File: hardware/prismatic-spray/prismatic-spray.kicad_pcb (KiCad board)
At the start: 2 copper layers, 205.3 x 86 mm, 17 parts, among them J1 Conn_01x03_Male, J2 Conn_01x03_Male, SW1 SW_Push, SW2 SW_Push, SW3 SW_Push, SW4 SW_Push, SW5 RotaryEncoder_Switch, U1 Pico

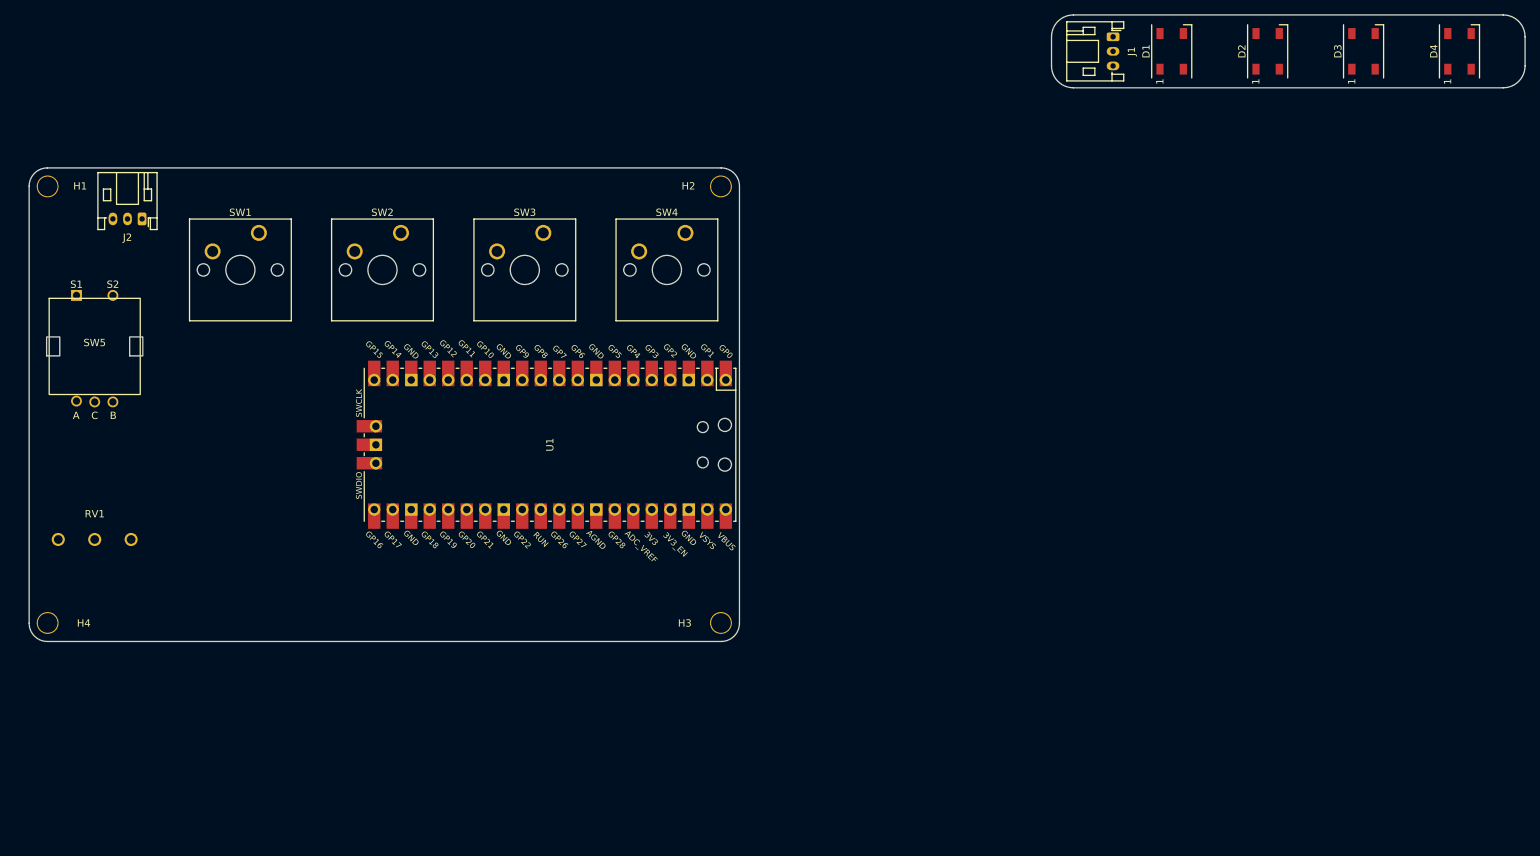
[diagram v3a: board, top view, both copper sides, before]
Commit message: Route most traces
- Route most traces on main board and daughter board
- Add mounting holes to daughter board
- Flip daughterboard connector to back of PCB
- Reassign some GPIOs for better routing
- Fix footprint for pec11 to get clean DRC
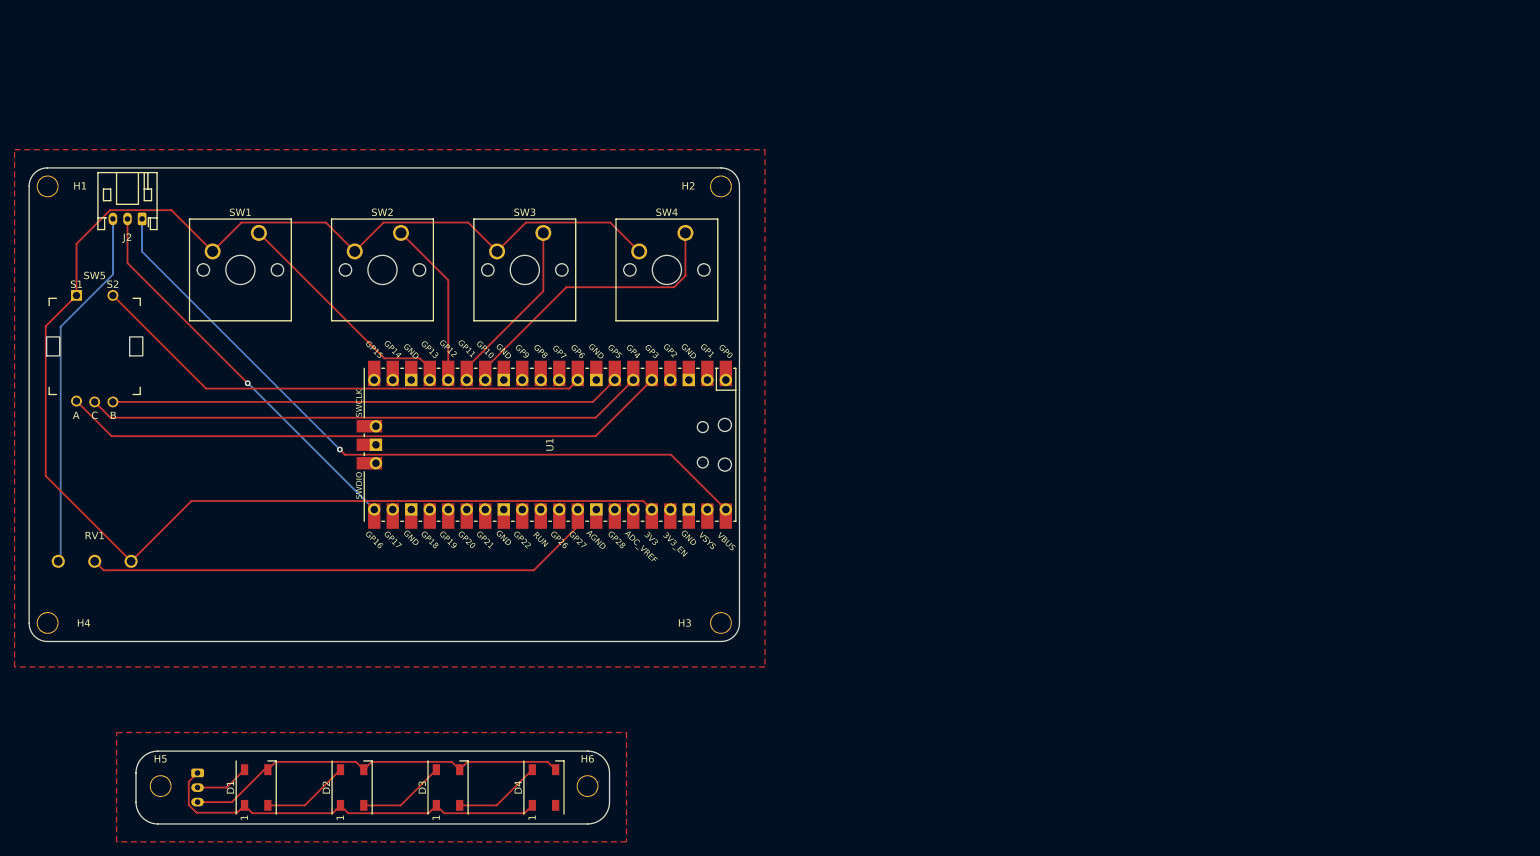
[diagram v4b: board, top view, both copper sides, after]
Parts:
- added H5: MountingHole, MountingHole:MountingHole_2.7mm_M2.5, F.Cu at (53.0, 125.3)
- added H6: MountingHole, MountingHole:MountingHole_2.7mm_M2.5, F.Cu at (111.7, 125.3)
- J1: moved to B.Cu
- moved D1 161.3 mm to (66.2, 125.5)
- moved D2 161.3 mm to (79.3, 125.5)
- moved D4 161.3 mm to (105.7, 125.5)
- moved D3 161.3 mm to (92.5, 125.5)
- moved J1 161.3 mm to (58.1, 123.5)
- moved RV1 3.00 mm to (44.0, 94.5)
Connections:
- net Net-(D1-Pad1) renamed /5V_B
- net Net-(D1-Pad3) renamed /GND_B
- D1 pad 4: /DATA -> /DATA_B
- J1 pad 2: /DATA -> /DATA_B
- J2 pad 1: +5V -> /5V_A
- J2 pad 2: /DATA -> /DATA_A
- SW5 pad A: Net-(U1-Pad7) -> Net-(U1-Pad5)
- SW5 pad B: Net-(U1-Pad5) -> Net-(U1-Pad7)
- SW5 pad S2: Net-(U1-Pad4) -> Net-(U1-Pad9)
- U1 pad 21: /DATA -> /DATA_A
- U1 pad 36: unconnected-(U1-Pad36) -> +3V3
- U1 pad 38: GND -> unconnected-(U1-Pad38)
- U1 pad 4: Net-(U1-Pad4) -> unconnected-(U1-Pad4)
- U1 pad 40: unconnected-(U1-Pad40) -> /5V_A
- U1 pad 9: unconnected-(U1-Pad9) -> Net-(U1-Pad9)
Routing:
- net +3V3: track 0.00 -> 216.9 mm
- net /5V_A: track 0.00 -> 99.3 mm, vias 0 -> 1
- net Net-(U1-Pad5): track 0.00 -> 84.2 mm
- net Net-(U1-Pad6): track 0.00 -> 77.0 mm
- net Net-(RV1-Pad2): track 0.00 -> 71.6 mm
- net Net-(U1-Pad7): track 0.00 -> 70.1 mm
- net Net-(U1-Pad9): track 0.00 -> 69.6 mm
- net /5V_B: track 0.00 -> 55.6 mm
- net /DATA_A: track 0.00 -> 53.9 mm, vias 0 -> 1
- net /GND_B: track 0.00 -> 53.7 mm
- net GND: track 0.00 -> 50.1 mm
- net Net-(SW4-Pad1): track 0.00 -> 40.2 mm
- net Net-(SW1-Pad1): track 0.00 -> 32.8 mm
- net Net-(SW3-Pad1): track 0.00 -> 24.5 mm
- net Net-(SW2-Pad1): track 0.00 -> 22.9 mm
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- added copper zone on F.Cu, net GND
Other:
- board size 205.3 x 86 mm -> 97.5 x 90.1 mm

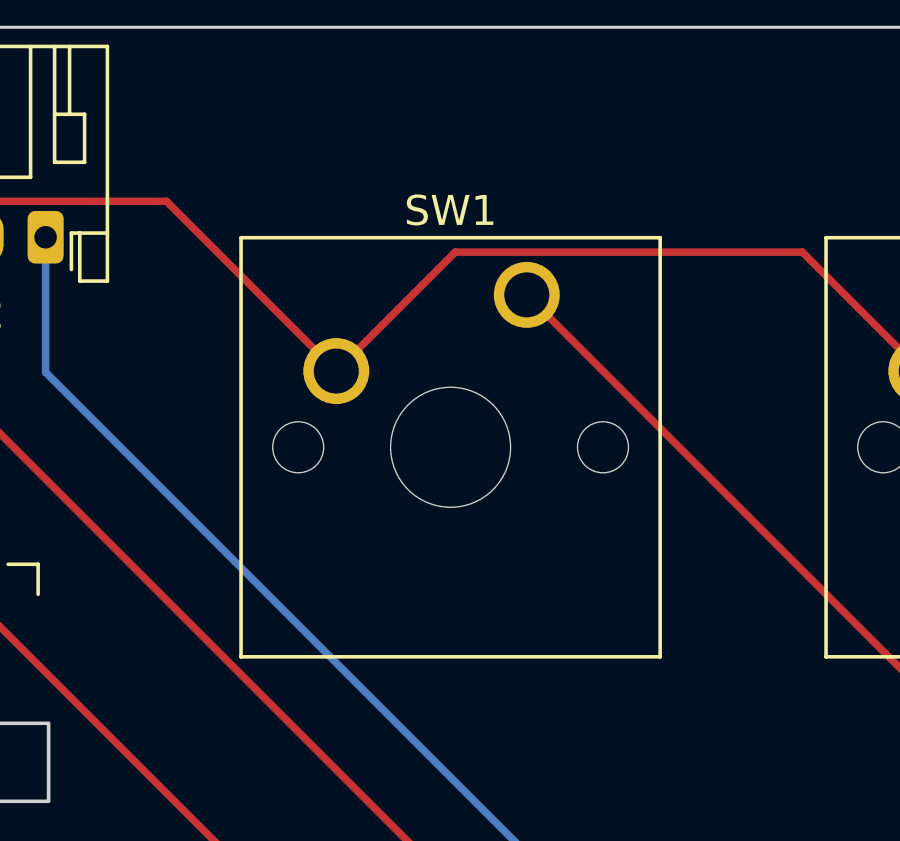
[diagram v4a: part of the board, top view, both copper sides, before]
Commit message: Add dimentions to PCB
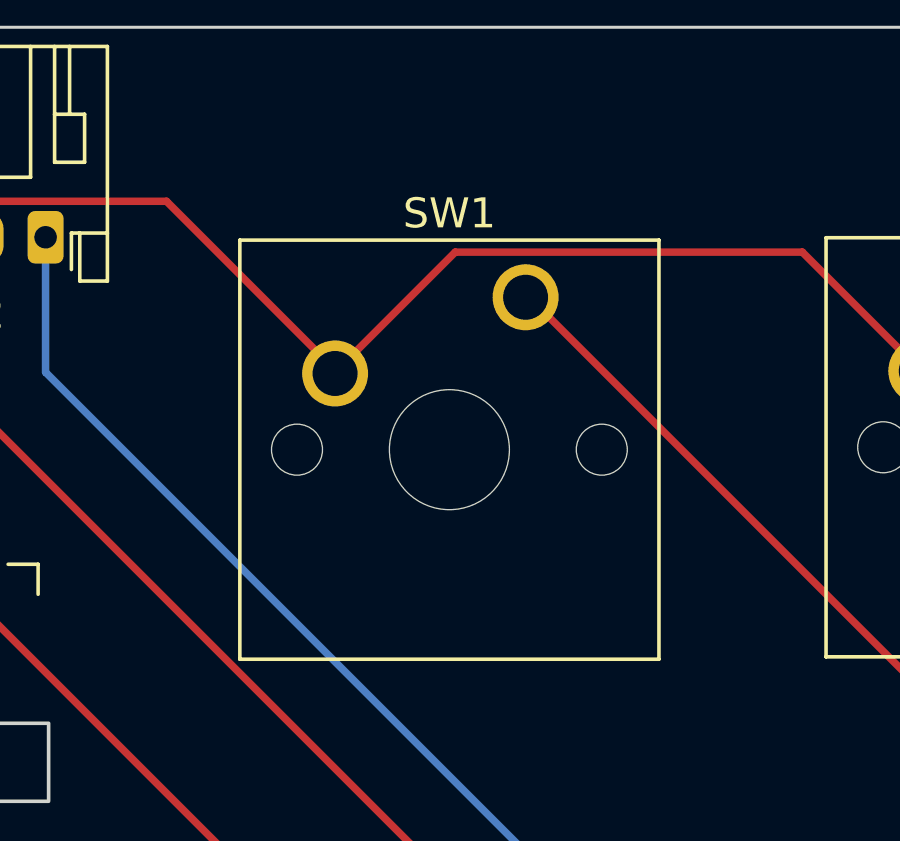
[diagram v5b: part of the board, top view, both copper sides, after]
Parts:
- moved SW1 0.09 mm to (66.5, 49.5)
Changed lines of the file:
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@@
   )
   (footprint "Button_Switch_Keyboard:SW_Cherry_MX_1.00u_PCB" (layer "F.Cu")
-    (at 66.54 49.42)
+    (at 66.5 49.5)
     (descr "Cherry MX keyswitch, 1.00u, PCB mount, http://cherryamericas.com/wp-content/uploads/2014/12/mx_cat.pdf")
     (tags "Cherry MX keyswitch 1.00u PCB")
@@
   (gr_arc (start 130 40.5) (mid 131.767767 41.232233) (end 132.5 43) (layer "Edge.Cuts") (width 0.1))
   (gr_arc (start 37.5 105.5) (mid 35.732233 104.767767) (end 35 103) (layer "Edge.Cuts") (width 0.1))
+  (dimension (type aligned) (layer "F.Cu")
+    (pts (xy 63.96 54.58) (xy 35.052 54.61))
+    (height 21.83977)
+    (gr_text "28.9080 mm" (at 49.481467 30.955243 0.05946010683) (layer "F.Cu")
+      (effects (font (size 1.5 1.5) (thickness 0.3)))
+    )
+    (format (units 3) (units_format 1) (precision 4))
+    (style (thickness 0.2) (arrow_length 1.27) (text_position_mode 0) (extension_height 0.58642) (extension_offset 0.5) keep_text_aligned)
+  )
   (segment (start 72.833334 128) (end 77.733334 123.1) (width 0.25) (layer "F.Cu") (net 1))
   (segment (start 67.766668 128) (end 72.833334 128) (width 0.25) (layer "F.Cu") (net 1))

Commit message: PCB Rev 1
Hardware rev 1
- Main board
- Daughter board
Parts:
- removed D1, D2, D3, D4: WS2812B, LED_SMD:LED_WS2812B_PLCC4_5.0x5.0mm_P3.2mm
- removed H5, H6: MountingHole, MountingHole:MountingHole_2.7mm_M2.5
- removed J1: Conn_01x03_Male, Connector_JST:JST_PH_S3B-PH-K_1x03_P2.00mm_Horizontal
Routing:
- net /5V_B: track 55.6 -> 0.00 mm
- net /GND_B: track 53.7 -> 0.00 mm
- net Net-(D3-Pad2): track 12.0 -> 0.00 mm
- net Net-(D2-Pad2): track 12.0 -> 0.00 mm
- net Net-(D1-Pad2): track 12.0 -> 0.00 mm
- net /DATA_B: track 7.46 -> 0.00 mm
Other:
- board size 97.5 x 90.1 mm -> 97.5 x 65 mm

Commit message: Add rendered image
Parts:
- moved RV1 111.0 mm to (8.72, -10.7)
- moved SW2 111.0 mm to (50.8, -55.8)
- moved SW3 111.0 mm to (70.3, -55.8)
- moved SW4 111.0 mm to (89.8, -55.8)
- moved U1 111.0 mm to (71.2, -26.7)
- moved H1 111.0 mm to (2.26, -62.2)
- moved H2 111.0 mm to (94.7, -62.2)
- moved H3 111.0 mm to (94.7, -2.26)
- moved H4 111.0 mm to (2.26, -2.26)
- moved J2 111.0 mm to (15.2, -57.7)
- moved SW1 111.0 mm to (31.2, -55.7)
- moved SW5 111.0 mm to (8.72, -40.2)

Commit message: finished case
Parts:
- moved H1 160.6 mm to (101.5, 64.0)
- moved H2 160.6 mm to (194.0, 64.0)
- moved RV1 160.6 mm to (108.0, 115.5)
- moved SW2 160.6 mm to (150.0, 70.4)
- moved SW3 160.6 mm to (169.6, 70.4)
- moved SW4 160.6 mm to (189.1, 70.4)
- moved U1 160.6 mm to (170.5, 99.5)
- moved H3 160.6 mm to (194.0, 124.0)
- moved H4 160.6 mm to (101.5, 124.0)
- moved J2 160.6 mm to (114.5, 68.5)
- moved SW1 160.6 mm to (130.5, 70.5)
- moved SW5 160.6 mm to (108.0, 86.0)
